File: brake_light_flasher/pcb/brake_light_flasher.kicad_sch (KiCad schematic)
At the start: 19 parts

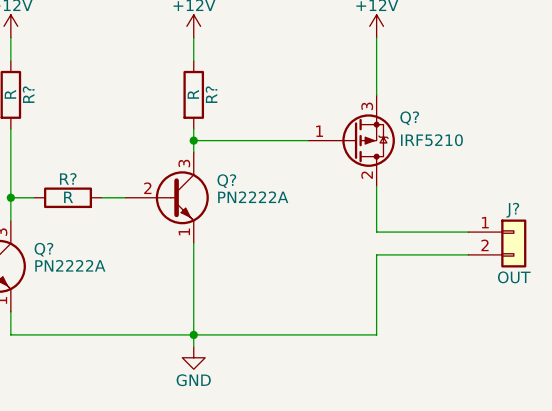
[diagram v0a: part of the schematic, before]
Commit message: add output diode
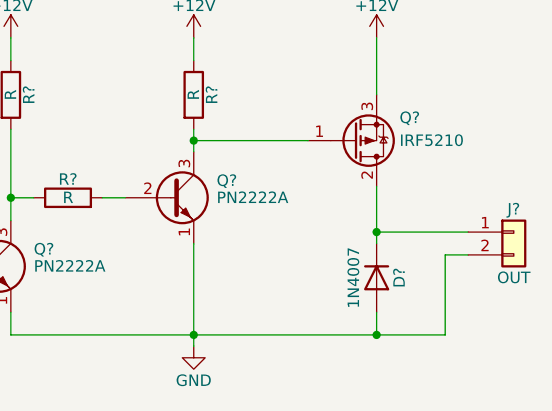
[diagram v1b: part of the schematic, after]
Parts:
- added D?: 1N4007, Diode_THT:D_DO-41_SOD81_P10.16mm_Horizontal, symbol Diode:1N4007
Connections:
- net GND: now also D?.2 (A)
- net at J?.1 (Pin_1), Q?.2 (D): now also D?.1 (K)
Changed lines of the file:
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@@
   (junction (at 113.03 82.55) (diameter 0) (color 0 0 0 0)
   )
+  (junction (at 210.82 147.32) (diameter 0) (color 0 0 0 0)
+  )
   (junction (at 170.18 132.08) (diameter 0) (color 0 0 0 0)
+  )
+  (junction (at 210.82 135.89) (diameter 0) (color 0 0 0 0)
   )
   (junction (at 146.05 69.85) (diameter 0) (color 0 0 0 0)
@@
     (stroke (width 0) (type default) (color 0 0 0 0))
   )
-  (wire (pts (xy 220.98 138.43) (xy 210.82 138.43))
+  (wire (pts (xy 220.98 138.43) (xy 218.44 138.43))
     (stroke (width 0) (type default) (color 0 0 0 0))
   )
@@
     (stroke (width 0) (type default) (color 0 0 0 0))
   )
+  (wire (pts (xy 210.82 135.89) (xy 210.82 137.16))
+    (stroke (width 0) (type default) (color 0 0 0 0))
+  )
   (wire (pts (xy 130.81 90.17) (xy 133.35 90.17))
     (stroke (width 0) (type default) (color 0 0 0 0))
@@
     (stroke (width 0) (type default) (color 0 0 0 0))
   )
+  (wire (pts (xy 210.82 147.32) (xy 190.5 147.32))
+    (stroke (width 0) (type default) (color 0 0 0 0))
+  )
   (wire (pts (xy 127 36.83) (xy 127 39.37))
     (stroke (width 0) (type default) (color 0 0 0 0))
@@
     (stroke (width 0) (type default) (color 0 0 0 0))
   )
+  (wire (pts (xy 210.82 144.78) (xy 210.82 147.32))
+    (stroke (width 0) (type default) (color 0 0 0 0))
+  )
   (wire (pts (xy 107.95 67.31) (xy 107.95 69.85))
     (stroke (width 0) (type default) (color 0 0 0 0))
   )
-  (wire (pts (xy 210.82 138.43) (xy 210.82 147.32))
+  (wire (pts (xy 218.44 138.43) (xy 218.44 147.32))
     (stroke (width 0) (type default) (color 0 0 0 0))
   )
@@
     (stroke (width 0) (type default) (color 0 0 0 0))
   )
-  (wire (pts (xy 210.82 147.32) (xy 190.5 147.32))
+  (wire (pts (xy 218.44 147.32) (xy 210.82 147.32))
     (stroke (width 0) (type default) (color 0 0 0 0))
   )
@@
     )
     (property "Datasheet" "~" (id 3) (at 156.21 139.7 0)
+      (effects (font (size 1.27 1.27)) hide)
+    )
+    (pin "1")
+    (pin "2")
+  )
+  (symbol (lib_id "Diode:1N4007") (at 210.82 140.97 270) (unit 1)
+    (in_bom yes) (on_board yes)
+    (property "Reference" "D?" (id 0) (at 213.36 140.97 0))
+    (property "Value" "1N4007" (id 1) (at 208.28 140.97 0))
+    (property "Footprint" "Diode_THT:D_DO-41_SOD81_P10.16mm_Horizontal" (id 2) (at 206.375 140.97 0)
+      (effects (font (size 1.27 1.27)) hide)
+    )
+    (property "Datasheet" "http://www.vishay.com/docs/88503/1n4001.pdf" (id 3) (at 210.82 140.97 0)
       (effects (font (size 1.27 1.27)) hide)
     )
@@
       (reference "C?") (unit 1) (value "1u") (footprint "")
     )
+    (path "/5ec234d4-9abe-45c2-816c-748e9134e8b0"
+      (reference "D?") (unit 1) (value "1N4007") (footprint "Diode_THT:D_DO-41_SOD81_P10.16mm_Horizontal")
+    )
     (path "/533872d6-63df-494e-b082-232d9ec7fd05"
